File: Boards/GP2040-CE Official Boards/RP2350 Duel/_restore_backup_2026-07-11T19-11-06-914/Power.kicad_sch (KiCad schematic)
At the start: 13 parts, among them J1 UJ20-C-H-G-SMT-2A-P16-TR, U4 TVS2200DRV, U5 24LC512, U6 TPD4EUSB30, U7 TPS25751SRSMR

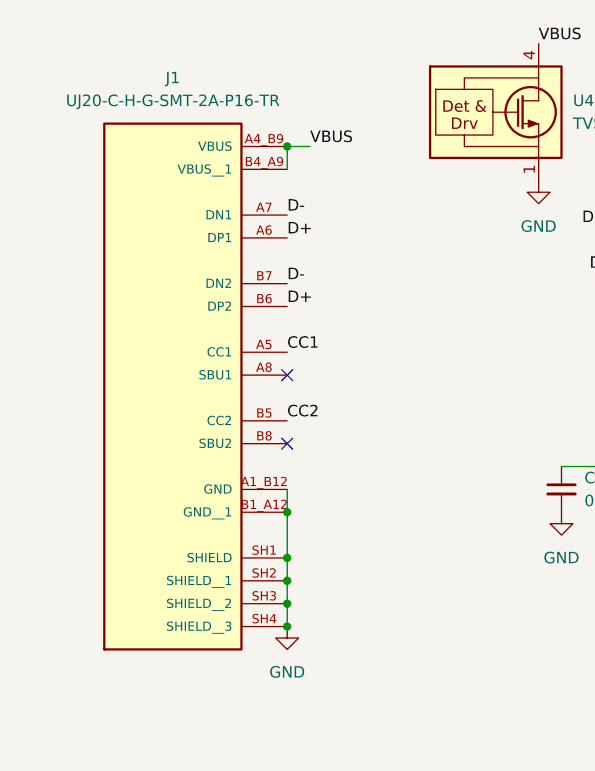
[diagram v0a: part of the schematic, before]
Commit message: Add fp-lib-table for GP2040-CE and RP2350 Duel libraries
- Created a new fp-lib-table file to include the GP2040-CE_Library and RP2350Duel libraries.
- Specified library URIs and types for integration with KiCad.
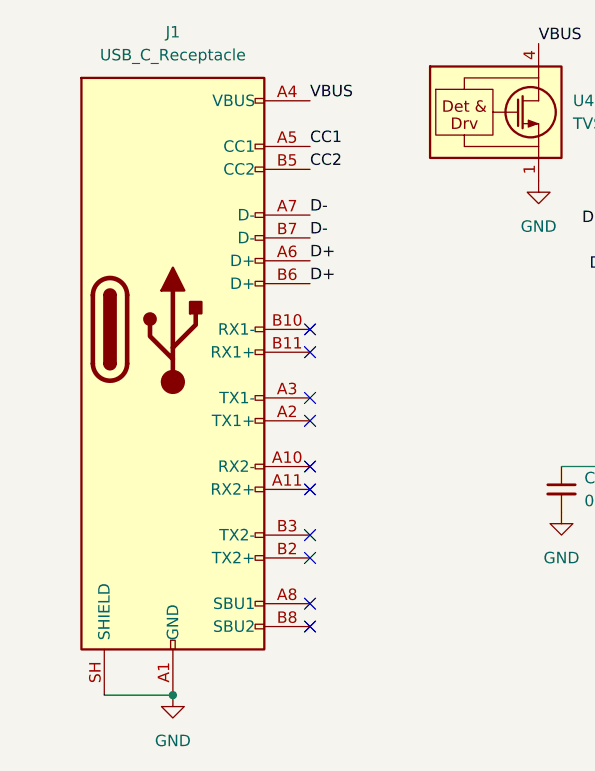
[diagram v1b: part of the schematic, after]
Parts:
- J1: value UJ20-C-H-G-SMT-2A-P16-TR -> USB_C_Receptacle; footprint RP2350Duel:SAMESKY_UJ20-C-H-G-SMT-2A-P16-TR -> Connector_USB:USB_C_Plug_Molex_105444; symbol RP2350Duel:UJ20-C-H-G-SMT-2A-P16-TR -> Connector:USB_C_Receptacle; CREATOR ASHISH -> (none); MANUFACTURER Same Sky -> (none); MAXIMUM_PACKAGE_HEIGHT 3.20mm -> (none); PARTREV 1.0 -> (none); STANDARD Manufacturer Recommendations -> (none); UNIT mm -> (none)
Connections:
- net GND: now also J1.A1 (GND), J1.A12 (GND), J1.B1 (GND), J1.B12 (GND), J1.SH (SHIELD); no longer J1.A1_B12 (GND), J1.B1_A12 (GND__1), J1.SH1 (SHIELD), J1.SH2 (SHIELD__1), J1.SH3 (SHIELD__2), J1.SH4 (SHIELD__3)
- net VBUS: now also J1.A4 (VBUS), J1.A9 (VBUS), J1.B4 (VBUS), J1.B9 (VBUS); no longer J1.A4_B9 (VBUS), J1.B4_A9 (VBUS__1)
- no-connect marks 9 -> 17
